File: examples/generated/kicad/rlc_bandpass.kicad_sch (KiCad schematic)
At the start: 5 parts

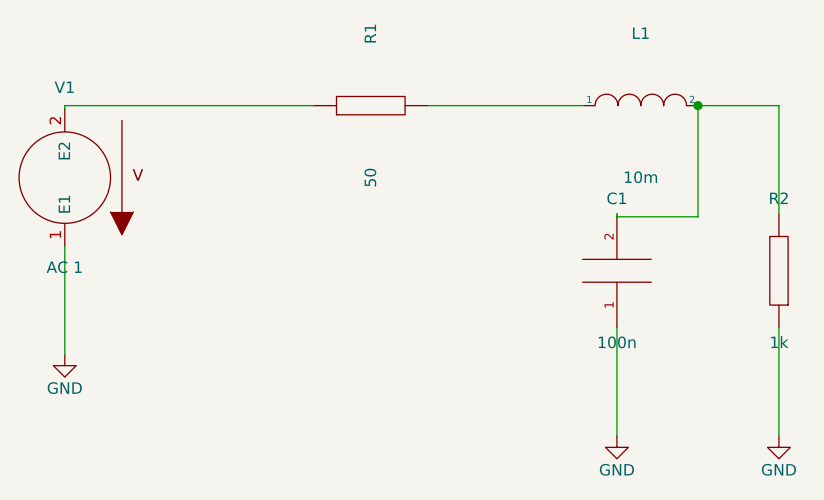
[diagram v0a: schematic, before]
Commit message: Ensure connectivity matches, as measured by opamp connectivity.
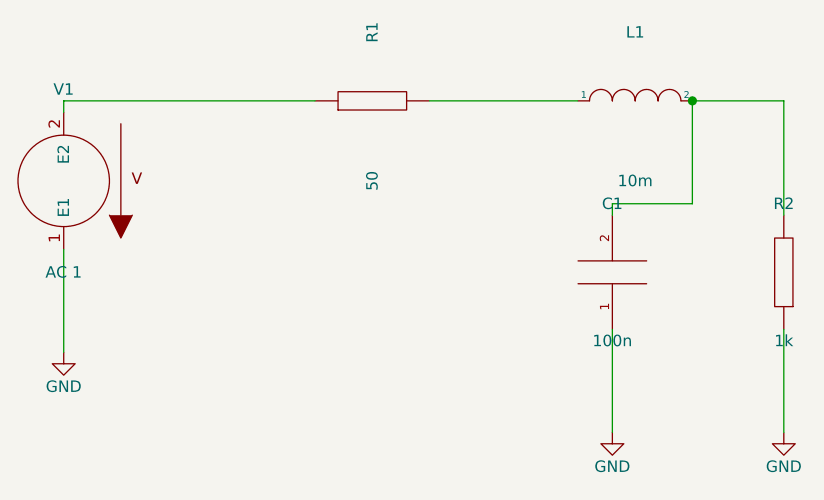
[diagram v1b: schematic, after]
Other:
- moved on the sheet: C1, L1, R1, R2
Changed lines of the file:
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@@
     (comment 1 "Generated by mixedsig2cad")
   )
-  (symbol (lib_id "VSOURCE") (at 56.00 86.00 180) (unit 1)
+  (symbol (lib_id "VSOURCE") (at 55.88 86.36 180) (unit 1)
     (in_bom yes) (on_board yes)
-    (property "Reference" "V1" (at 56.0 76.0 0)
+    (property "Reference" "V1" (at 55.88 76.2 0)
       (effects (font (size 1.27 1.27)))
     )
-    (property "Value" "AC 1" (at 56.0 96.0 0)
+    (property "Value" "AC 1" (at 55.88 96.52 0)
       (effects (font (size 1.27 1.27)))
     )
@@
     )
   )
-  (symbol (lib_id "GND") (at 56.00 105.62 0) (unit 1)
+  (symbol (lib_id "GND") (at 55.88 105.41 0) (unit 1)
     (in_bom yes) (on_board yes)
-    (property "Reference" "#PWR0001" (at 56.0 101.81 0)
+    (property "Reference" "#PWR0001" (at 55.88 101.6 0)
       (effects (font (size 1.27 1.27)) hide)
     )
-    (property "Value" "GND" (at 56.0 109.43 0)
+    (property "Value" "GND" (at 55.88 109.22 0)
       (effects (font (size 1.27 1.27)))
     )
@@
     )
   )
-  (symbol (lib_id "R") (at 90.00 78.00 90) (unit 1)
+  (symbol (lib_id "R") (at 90.17 77.47 90) (unit 1)
     (in_bom yes) (on_board yes)
-    (property "Reference" "R1" (at 90.0 70.0 0)
+    (property "Reference" "R1" (at 90.17 69.85 0)
       (effects (font (size 1.27 1.27)))
     )
-    (property "Value" "50" (at 90.0 86.0 0)
+    (property "Value" "50" (at 90.17 86.36 0)
       (effects (font (size 1.27 1.27)))
     )
@@
     )
   )
-  (symbol (lib_id "INDUCTOR") (at 120.00 78.00 0) (unit 1)
+  (symbol (lib_id "INDUCTOR") (at 119.38 77.47 0) (unit 1)
     (in_bom yes) (on_board yes)
-    (property "Reference" "L1" (at 120.0 70.0 0)
+    (property "Reference" "L1" (at 119.38 69.85 0)
       (effects (font (size 1.27 1.27)))
     )
-    (property "Value" "10m" (at 120.0 86.0 0)
+    (property "Value" "10m" (at 119.38 86.36 0)
       (effects (font (size 1.27 1.27)))
     )
@@
     )
   )
-  (symbol (lib_id "CAP") (at 117.35 96.35 180) (unit 1)
+  (symbol (lib_id "CAP") (at 116.84 96.52 180) (unit 1)
     (in_bom yes) (on_board yes)
-    (property "Reference" "C1" (at 117.35 88.35 0)
+    (property "Reference" "C1" (at 116.84 88.9 0)
       (effects (font (size 1.27 1.27)))
     )
-    (property "Value" "100n" (at 117.35 104.35 0)
+    (property "Value" "100n" (at 116.84 104.14 0)
       (effects (font (size 1.27 1.27)))
     )
@@
     )
   )
-  (symbol (lib_id "GND") (at 117.35 114.70 0) (unit 1)
+  (symbol (lib_id "GND") (at 116.84 114.30 0) (unit 1)
     (in_bom yes) (on_board yes)
-    (property "Reference" "#PWR0002" (at 117.35 110.89 0)
+    (property "Reference" "#PWR0002" (at 116.84 110.49 0)
       (effects (font (size 1.27 1.27)) hide)
     )
-    (property "Value" "GND" (at 117.35 118.51 0)
+    (property "Value" "GND" (at 116.84 118.11 0)
       (effects (font (size 1.27 1.27)))
     )
@@
     )
   )
-  (symbol (lib_id "R") (at 135.35 96.35 180) (unit 1)
+  (symbol (lib_id "R") (at 135.89 96.52 180) (unit 1)
     (in_bom yes) (on_board yes)
-    (property "Reference" "R2" (at 135.35 88.35 0)
+    (property "Reference" "R2" (at 135.89 88.9 0)
       (effects (font (size 1.27 1.27)))
     )
-    (property "Value" "1k" (at 135.35 104.35 0)
+    (property "Value" "1k" (at 135.89 104.14 0)
       (effects (font (size 1.27 1.27)))
     )
@@
     )
   )
-  (symbol (lib_id "GND") (at 135.35 114.70 0) (unit 1)
+  (symbol (lib_id "GND") (at 135.89 114.30 0) (unit 1)
     (in_bom yes) (on_board yes)
-    (property "Reference" "#PWR0003" (at 135.35 110.89 0)
+    (property "Reference" "#PWR0003" (at 135.89 110.49 0)
       (effects (font (size 1.27 1.27)) hide)
     )
-    (property "Value" "GND" (at 135.35 118.51 0)
+    (property "Value" "GND" (at 135.89 118.11 0)
       (effects (font (size 1.27 1.27)))
     )
@@
     )
   )
-  (wire (pts (xy 117.35 102.70) (xy 117.35 114.70))
+  (wire (pts (xy 116.84 102.87) (xy 116.84 114.30))
     (stroke (width 0) (type solid) (color 0 0 0 0))
   )
-  (wire (pts (xy 135.35 102.70) (xy 135.35 114.70))
+  (wire (pts (xy 135.89 102.87) (xy 135.89 114.30))
     (stroke (width 0) (type solid) (color 0 0 0 0))
   )
-  (wire (pts (xy 56.00 93.62) (xy 56.00 105.62))
+  (wire (pts (xy 55.88 93.98) (xy 55.88 105.41))
     (stroke (width 0) (type solid) (color 0 0 0 0))
   )
-  (wire (pts (xy 56.00 78.38) (xy 56.00 78.00))
+  (wire (pts (xy 55.88 78.74) (xy 55.88 77.47))
     (stroke (width 0) (type solid) (color 0 0 0 0))
   )
-  (wire (pts (xy 56.00 78.00) (xy 83.65 78.00))
+  (wire (pts (xy 55.88 77.47) (xy 83.82 77.47))
     (stroke (width 0) (type solid) (color 0 0 0 0))
   )
-  (wire (pts (xy 96.35 78.00) (xy 113.65 78.00))
+  (wire (pts (xy 96.52 77.47) (xy 113.03 77.47))
     (stroke (width 0) (type solid) (color 0 0 0 0))
   )
-  (wire (pts (xy 117.35 90.00) (xy 117.35 90.35))
+  (wire (pts (xy 116.84 90.17) (xy 116.84 88.90))
     (stroke (width 0) (type solid) (color 0 0 0 0))
   )
-  (wire (pts (xy 117.35 90.35) (xy 126.35 90.35))
+  (wire (pts (xy 116.84 88.90) (xy 125.73 88.90))
     (stroke (width 0) (type solid) (color 0 0 0 0))
   )
-  (wire (pts (xy 126.35 90.35) (xy 126.35 78.00))
+  (wire (pts (xy 125.73 88.90) (xy 125.73 77.47))
     (stroke (width 0) (type solid) (color 0 0 0 0))
   )
-  (wire (pts (xy 135.35 90.00) (xy 135.35 78.00))
+  (wire (pts (xy 135.89 90.17) (xy 135.89 77.47))
     (stroke (width 0) (type solid) (color 0 0 0 0))
   )
-  (wire (pts (xy 135.35 78.00) (xy 126.35 78.00))
+  (wire (pts (xy 135.89 77.47) (xy 125.73 77.47))
     (stroke (width 0) (type solid) (color 0 0 0 0))
   )
-  (junction (at 126.35 78.00) (diameter 1.016) (color 0 0 0 0))
+  (junction (at 125.73 77.47) (diameter 1.016) (color 0 0 0 0))
   (sheet_instances
     (path "/" (page "1"))

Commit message: Refactor further.
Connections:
- net vin: now reaches R1.1, V1.2 (E2)
- net n1: now reaches L1.1, R1.2
- net n2: now reaches C1.2, L1.2, R2.2
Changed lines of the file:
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@@
     )
+  )
+  (label "vin" (at 69.85 77.47 0)
+    (effects (font (size 1.27 1.27)))
+  )
+  (label "n1" (at 96.52 77.47 0)
+    (effects (font (size 1.27 1.27)))
+  )
+  (label "n2" (at 125.73 77.47 0)
+    (effects (font (size 1.27 1.27)))
   )
   (wire (pts (xy 116.84 102.87) (xy 116.84 114.30))

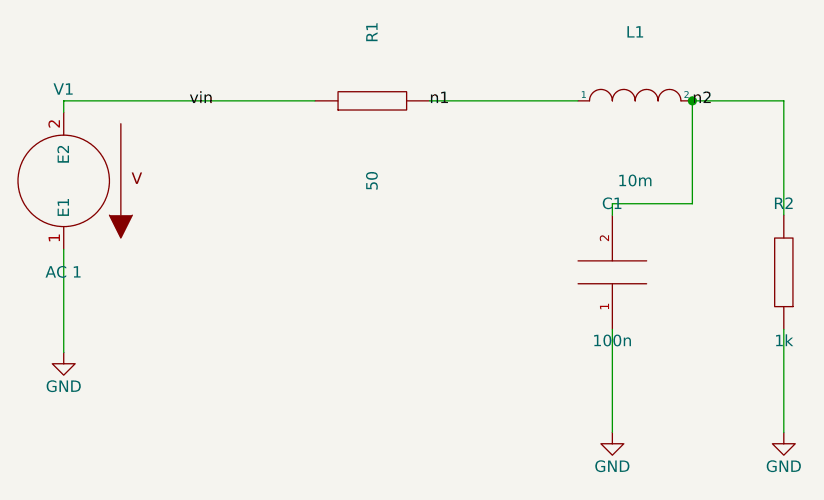
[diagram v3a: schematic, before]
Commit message: Attempt to add the right connections for the schmitt trigger. Messed up cmos inverter.
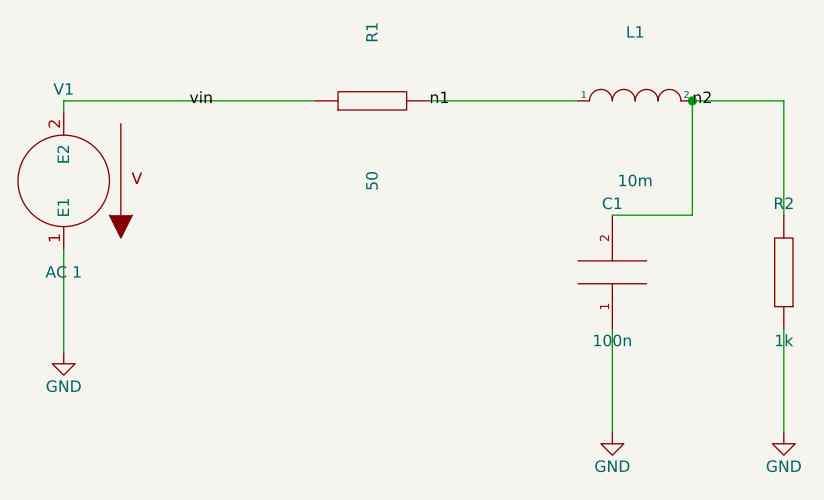
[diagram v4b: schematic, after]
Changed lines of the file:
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@@
   (title_block
     (title "rlc_bandpass")
-    (date "2026-03-13")
+    (date "2026-03-14")
     (comment 1 "Generated by mixedsig2cad")
   )
@@
     (stroke (width 0) (type solid) (color 0 0 0 0))
   )
-  (wire (pts (xy 116.84 90.17) (xy 116.84 88.90))
+  (wire (pts (xy 116.84 90.17) (xy 125.73 90.17))
     (stroke (width 0) (type solid) (color 0 0 0 0))
   )
-  (wire (pts (xy 116.84 88.90) (xy 125.73 88.90))
+  (wire (pts (xy 125.73 90.17) (xy 125.73 77.47))
     (stroke (width 0) (type solid) (color 0 0 0 0))
   )
-  (wire (pts (xy 125.73 88.90) (xy 125.73 77.47))
-    (stroke (width 0) (type solid) (color 0 0 0 0))
-  )

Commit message: Fix CMOS inverter issue.
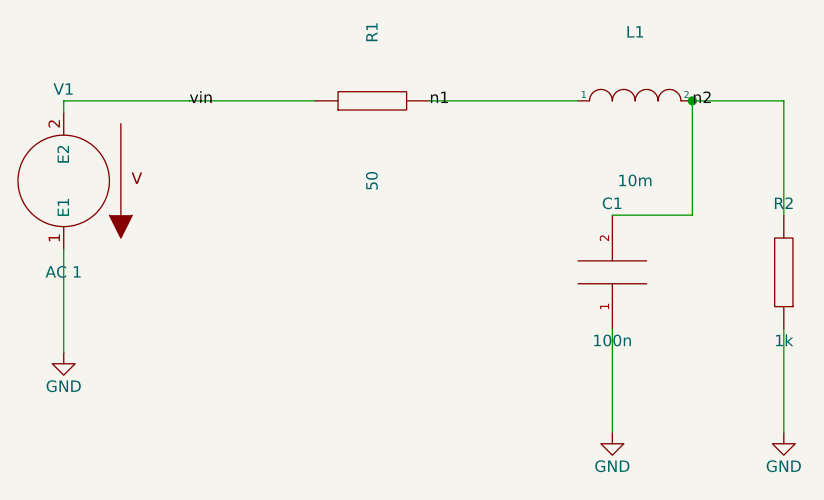
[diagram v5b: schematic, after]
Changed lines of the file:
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@@
     (stroke (width 0) (type solid) (color 0 0 0 0))
   )
-  (wire (pts (xy 55.88 77.47) (xy 83.82 77.47))
+  (wire (pts (xy 55.88 77.47) (xy 69.85 77.47))
     (stroke (width 0) (type solid) (color 0 0 0 0))
   )
-  (wire (pts (xy 96.52 77.47) (xy 113.03 77.47))
+  (wire (pts (xy 83.82 77.47) (xy 69.85 77.47))
     (stroke (width 0) (type solid) (color 0 0 0 0))
   )
+  (wire (pts (xy 113.03 77.47) (xy 96.52 77.47))
+    (stroke (width 0) (type solid) (color 0 0 0 0))
+  )

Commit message: Manually change schematics to match what I want.
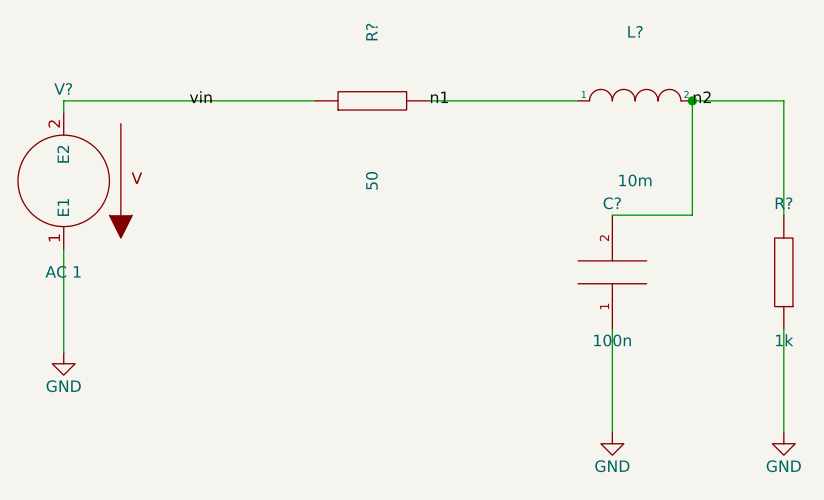
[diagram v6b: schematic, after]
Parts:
- renumbered C1 to C?, L1 to L?, R1 to R?, R2 to R?, V1 to V?

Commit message: Attempt to match manual schematics with seeded layout and generation.
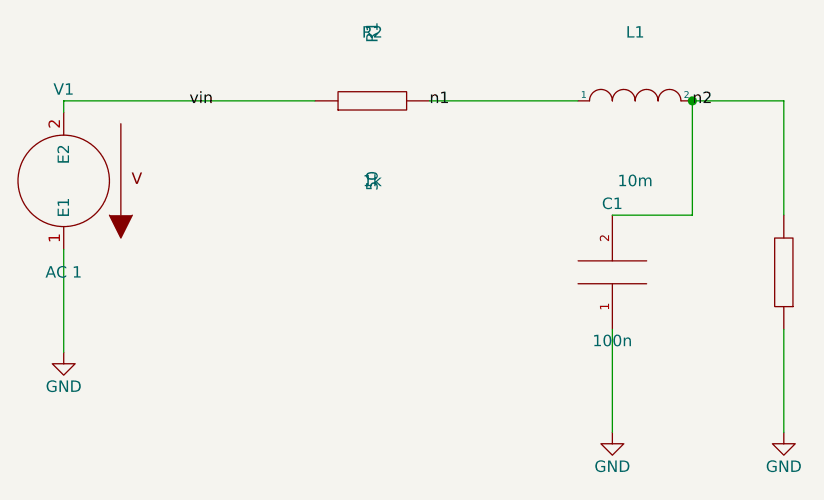
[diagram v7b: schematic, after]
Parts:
- gave numbers to parts that had none: 5
